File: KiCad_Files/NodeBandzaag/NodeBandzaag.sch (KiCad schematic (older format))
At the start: 38 parts, among them J1 AC Current In, J10 Opto Coupler 1 in, J13 Relay 1 Output, J2 Current coil in, J29 Current sensor select, J3 AC Current loop, J4 EXT1, J6 RFIDReader, J7 EXT2, J8 Force output Relay 1 on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

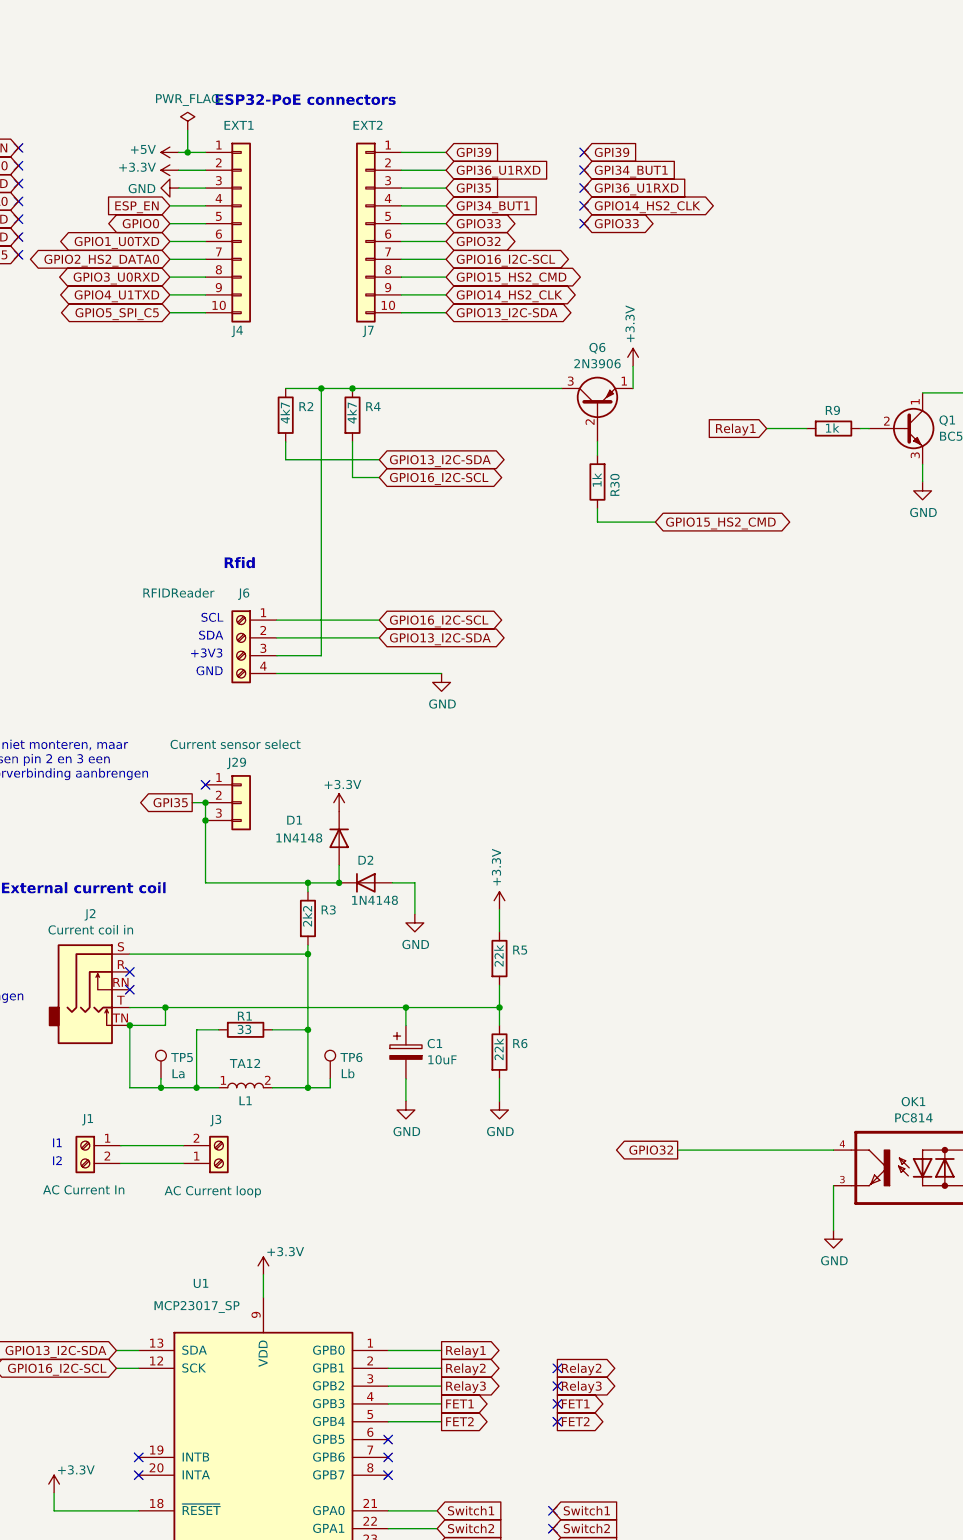
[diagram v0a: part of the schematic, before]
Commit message: V1.0.0.0 Updated the KiCad design and added the source code for the node
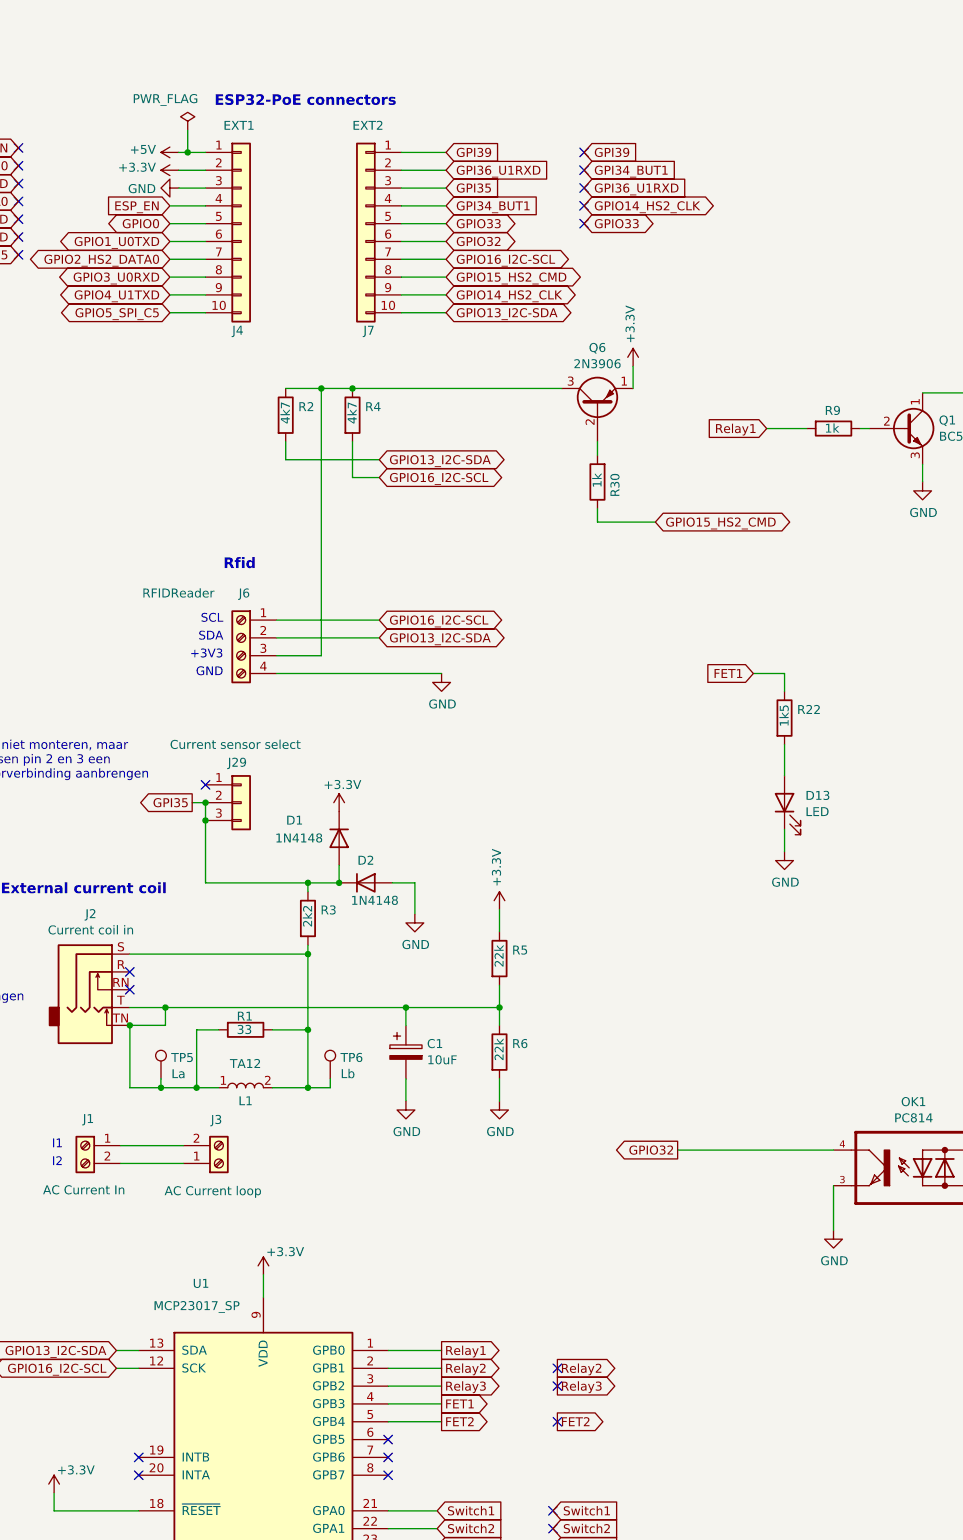
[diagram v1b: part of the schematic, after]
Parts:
- added D13: LED, LED_THT:LED_D3.0mm, symbol Device:LED
- added R22: 1k5, Resistor_THT:R_Axial_DIN0207_L6.3mm_D2.5mm_P7.62mm_Horizontal, symbol Device:R
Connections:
- net FET1: now also R22.1
- net GND: now also D13.1 (K)
- new net: D13.2 (A), R22.2
- no-connect marks 34 -> 33
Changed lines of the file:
@@
 Sheet 1 1
 Title "Node Bandzaag"
-Date "2021-12-08"
-Rev "V0.1"
+Date "2021-12-14"
+Rev "V0.3"
 Comp "MakerSpace Leiden"
 Comment1 "Getekend door: Hans Beerman"
@@
 P 5750 1325
 F 0 "#FLG0101" H 5750 1400 50  0001 C CNN
-F 1 "PWR_FLAG" H 5750 1500 50  0000 C CNN
+F 1 "PWR_FLAG" H 5625 1500 50  0000 C CNN
 F 2 "" H 5750 1325 50  0001 C CNN
 F 3 "~" H 5750 1325 50  0001 C CNN
@@
 Text GLabel 7825 8275 2    50   Output ~ 0
 Relay2
-Text GLabel 7825 8475 2    50   Output ~ 0
+Text GLabel 8925 4375 0    50   Input ~ 0
 FET1
 Text GLabel 7825 8575 2    50   Output ~ 0
@@
 NoConn ~ 7825 8275
 NoConn ~ 7825 8375
-NoConn ~ 7825 8475
 NoConn ~ 7825 8575
 Text GLabel 7800 9075 2    50   Input ~ 0
@@
 NoConn ~ 7800 9175
 NoConn ~ 7800 9275
+$Comp
+L Device:R R22
+U 1 1 61B66960
+P 9100 4625
+F 0 "R22" H 9170 4671 50  0000 L CNN
+F 1 "1k5" V 9100 4575 50  0000 L CNN
+F 2 "Resistor_THT:R_Axial_DIN0207_L6.3mm_D2.5mm_P7.62mm_Horizontal" V 9030 4625 50  0001 C CNN
+F 3 "~" H 9100 4625 50  0001 C CNN
+	1    9100 4625
+	1    0    0    -1
+$EndComp
+$Comp
+L Device:LED D13
+U 1 1 61B68196
+P 9100 5100
+F 0 "D13" V 9139 4983 50  0000 R CNN
+F 1 "LED" V 9048 4983 50  0000 R CNN
+F 2 "LED_THT:LED_D3.0mm" H 9100 5100 50  0001 C CNN
+F 3 "~" H 9100 5100 50  0001 C CNN
+	1    9100 5100
+	0    -1   -1   0
+$EndComp
+$Comp
+L power:GND #PWR0102
+U 1 1 61B68F30
+P 9100 5375
+F 0 "#PWR0102" H 9100 5125 50  0001 C CNN
+F 1 "GND" H 9105 5202 50  0000 C CNN
+F 2 "" H 9100 5375 50  0001 C CNN
+F 3 "" H 9100 5375 50  0001 C CNN
+	1    9100 5375
+	1    0    0    -1
+$EndComp
+Wire Wire Line
+	8925 4375 9100 4375
+Wire Wire Line
+	9100 4375 9100 4475
+Wire Wire Line
+	9100 4775 9100 4950
+Wire Wire Line
+	9100 5250 9100 5375
 $EndSCHEMATC
